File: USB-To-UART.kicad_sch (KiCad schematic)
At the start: 12 parts, among them Q1 NMOS, Q2 NMOS, U4 CH340X

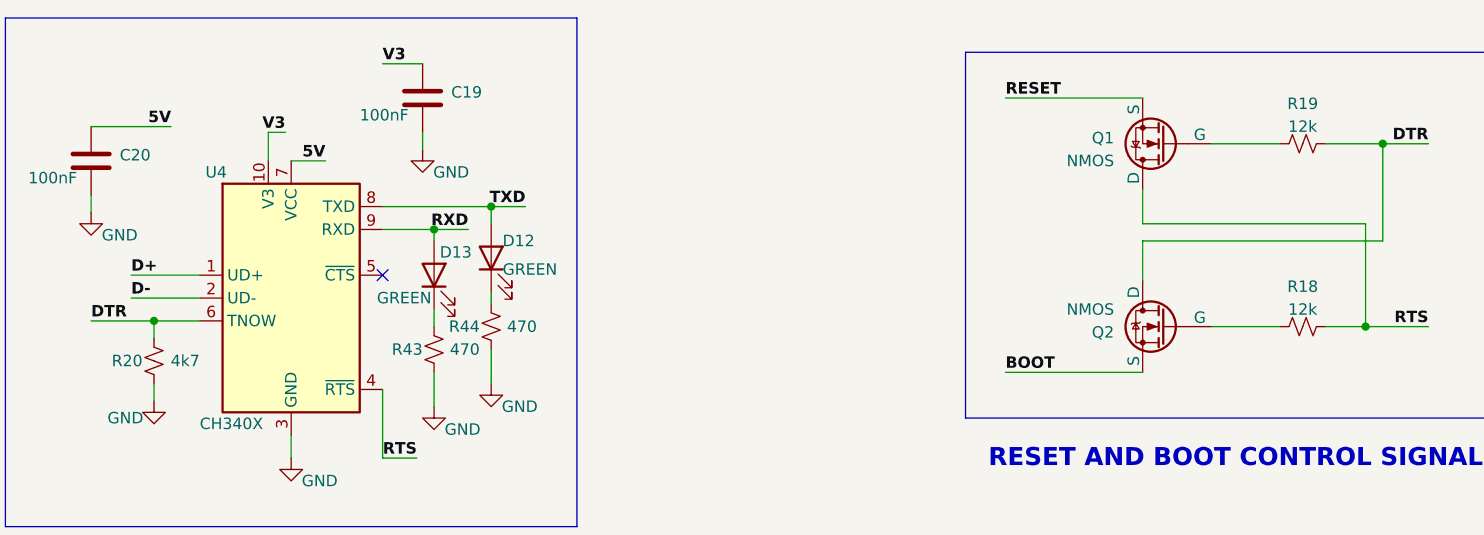
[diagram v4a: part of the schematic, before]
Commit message: Assigned footprints
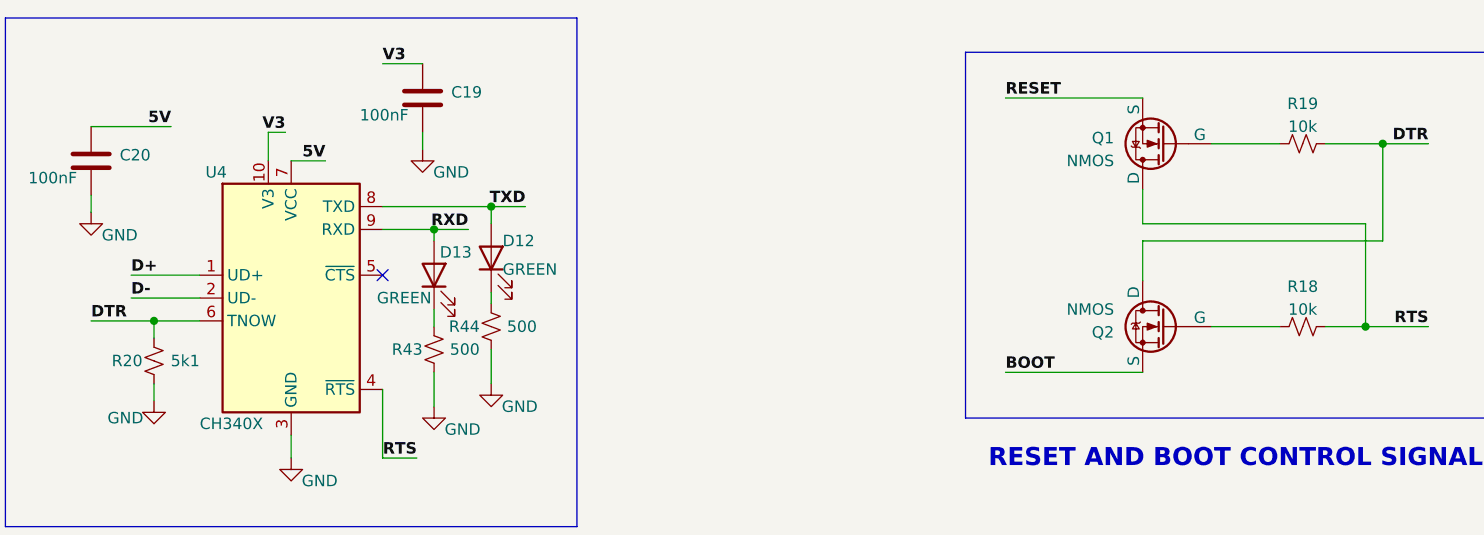
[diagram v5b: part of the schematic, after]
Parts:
- C19, C20: footprint ESP32-S3_DB:C_0402_1005Metric -> ESP32-S3_Dev_Board:C_0402_1005Metric
- D12, D13: footprint ESP32-S3_DB:LED_0603_1608Metric -> ESP32-S3_Dev_Board:LED_0603_1608Metric
- Q1, Q2: footprint (none) -> ESP32-S3_Dev_Board:SOT-23-3; PN (none) -> BSS138
- R18, R19: value 12k -> 10k; footprint (none) -> ESP32-S3_Dev_Board:R_0402_1005Metric; PN (none) -> RC0402FR-0710KL
- R20: value 4k7 -> 5k1; footprint (none) -> ESP32-S3_Dev_Board:R_0402_1005Metric; PN (none) -> RC0402FR-075K1L
- R43, R44: value 470 -> 500; footprint (none) -> ESP32-S3_Dev_Board:R_0402_1005Metric; PN (none) -> RC0402FR-07499RL
- U4: footprint Package_SO:MSOP-10_3x3mm_P0.5mm -> ESP32-S3_Dev_Board:MSOP-10_3x3mm_P0.5mm; PN (none) -> CH340X
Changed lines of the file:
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@@
       (effects (font (size 1.27 1.27)) (justify right))
     )
-    (property "Footprint" "ESP32-S3_DB:LED_0603_1608Metric" (at 116.84 95.885 0)
+    (property "Footprint" "ESP32-S3_Dev_Board:LED_0603_1608Metric" (at 116.84 95.885 0)
       (effects (font (size 1.27 1.27)) hide)
     )
@@
       (effects (font (size 1.27 1.27)) (justify left))
     )
-    (property "Value" "470" (at 128.27 101.6 0)
-      (effects (font (size 1.27 1.27)) (justify left))
-    )
-    (property "Footprint" "" (at 123.19 101.6 0)
+    (property "Value" "500" (at 128.27 101.6 0)
+      (effects (font (size 1.27 1.27)) (justify left))
+    )
+    (property "Footprint" "ESP32-S3_Dev_Board:R_0402_1005Metric" (at 123.19 101.6 0)
       (effects (font (size 1.27 1.27)) hide)
     )
@@
       (effects (font (size 1.27 1.27)) hide)
     )
+    (property "PN" "RC0402FR-07499RL" (at 123.19 101.6 0)
+      (effects (font (size 1.27 1.27)) hide)
+    )
     (pin "1")
     (pin "2")
@@
       (effects (font (size 1.27 1.27)) (justify left))
     )
-    (property "Value" "4k7" (at 90.805 105.41 0)
-      (effects (font (size 1.27 1.27)) (justify left))
-    )
-    (property "Footprint" "" (at 85.725 105.41 0)
+    (property "Value" "5k1" (at 90.805 105.41 0)
+      (effects (font (size 1.27 1.27)) (justify left))
+    )
+    (property "Footprint" "ESP32-S3_Dev_Board:R_0402_1005Metric" (at 85.725 105.41 0)
       (effects (font (size 1.27 1.27)) hide)
     )
@@
       (effects (font (size 1.27 1.27)) hide)
     )
+    (property "PN" "RC0402FR-075K1L" (at 85.725 105.41 0)
+      (effects (font (size 1.27 1.27)) hide)
+    )
     (pin "1")
     (pin "2")
@@
       (effects (font (size 1.27 1.27)) (justify left))
     )
-    (property "Value" "470" (at 121.92 104.14 0)
-      (effects (font (size 1.27 1.27)) (justify left))
-    )
-    (property "Footprint" "" (at 116.84 104.14 0)
+    (property "Value" "500" (at 121.92 104.14 0)
+      (effects (font (size 1.27 1.27)) (justify left))
+    )
+    (property "Footprint" "ESP32-S3_Dev_Board:R_0402_1005Metric" (at 116.84 104.14 0)
       (effects (font (size 1.27 1.27)) hide)
     )
@@
       (effects (font (size 1.27 1.27)) hide)
     )
+    (property "PN" "RC0402FR-07499RL" (at 116.84 104.14 0)
+      (effects (font (size 1.27 1.27)) hide)
+    )
     (pin "1")
     (pin "2")
@@
       (effects (font (size 1.27 1.27)) (justify left))
     )
-    (property "Footprint" "" (at 193.04 99.06 0)
+    (property "Footprint" "ESP32-S3_Dev_Board:SOT-23-3" (at 193.04 99.06 0)
       (effects (font (size 1.27 1.27)) hide)
     )
@@
     )
     (property "Sim.Pins" "1=D 2=G 3=S" (at 198.12 116.84 0)
+      (effects (font (size 1.27 1.27)) hide)
+    )
+    (property "PN" "BSS138" (at 198.12 101.6 0)
       (effects (font (size 1.27 1.27)) hide)
     )
@@
       (effects (font (size 1.27 1.27)) (justify left))
     )
-    (property "Footprint" "" (at 193.04 83.82 0)
+    (property "Footprint" "ESP32-S3_Dev_Board:SOT-23-3" (at 193.04 83.82 0)
       (effects (font (size 1.27 1.27)) hide)
     )
@@
     )
     (property "Sim.Pins" "1=D 2=G 3=S" (at 198.12 66.04 0)
+      (effects (font (size 1.27 1.27)) hide)
+    )
+    (property "PN" "BSS138" (at 198.12 81.28 0)
       (effects (font (size 1.27 1.27)) hide)
     )
@@
       (effects (font (size 1.27 1.27)))
     )
-    (property "Value" "12k" (at 213.36 79.375 90)
-      (effects (font (size 1.27 1.27)))
-    )
-    (property "Footprint" "" (at 213.36 81.28 0)
+    (property "Value" "10k" (at 213.36 79.375 90)
+      (effects (font (size 1.27 1.27)))
+    )
+    (property "Footprint" "ESP32-S3_Dev_Board:R_0402_1005Metric" (at 213.36 81.28 0)
       (effects (font (size 1.27 1.27)) hide)
     )
@@
       (effects (font (size 1.27 1.27)) hide)
     )
+    (property "PN" "RC0402FR-0710KL" (at 213.36 81.28 0)
+      (effects (font (size 1.27 1.27)) hide)
+    )
     (pin "1")
     (pin "2")
@@
       (effects (font (size 1.27 1.27)) (justify right))
     )
-    (property "Footprint" "ESP32-S3_DB:C_0402_1005Metric" (at 114.6048 72.39 0)
+    (property "Footprint" "ESP32-S3_Dev_Board:C_0402_1005Metric" (at 114.6048 72.39 0)
       (effects (font (size 1.27 1.27)) hide)
     )
@@
       (effects (font (size 1.27 1.27)))
     )
-    (property "Value" "12k" (at 213.36 99.695 90)
-      (effects (font (size 1.27 1.27)))
-    )
-    (property "Footprint" "" (at 213.36 101.6 0)
+    (property "Value" "10k" (at 213.36 99.695 90)
+      (effects (font (size 1.27 1.27)))
+    )
+    (property "Footprint" "ESP32-S3_Dev_Board:R_0402_1005Metric" (at 213.36 101.6 0)
       (effects (font (size 1.27 1.27)) hide)
     )
@@
       (effects (font (size 1.27 1.27)) hide)
     )
+    (property "PN" "RC0402FR-0710KL" (at 213.36 101.6 0)
+      (effects (font (size 1.27 1.27)) hide)
+    )
     (pin "1")
     (pin "2")
@@
       (effects (font (size 1.27 1.27)) (justify right))
     )
-    (property "Footprint" "ESP32-S3_DB:C_0402_1005Metric" (at 77.7748 79.375 0)
+    (property "Footprint" "ESP32-S3_Dev_Board:C_0402_1005Metric" (at 77.7748 79.375 0)
       (effects (font (size 1.27 1.27)) hide)
     )
@@
       (effects (font (size 1.27 1.27)) (justify right))
     )
-    (property "Footprint" "ESP32-S3_DB:LED_0603_1608Metric" (at 123.19 93.98 0)
+    (property "Footprint" "ESP32-S3_Dev_Board:LED_0603_1608Metric" (at 123.19 93.98 0)
       (effects (font (size 1.27 1.27)) hide)
     )
@@
       (effects (font (size 1.27 1.27)) (justify left))
     )
-    (property "Footprint" "Package_SO:MSOP-10_3x3mm_P0.5mm" (at 102.235 112.395 0)
+    (property "Footprint" "ESP32-S3_Dev_Board:MSOP-10_3x3mm_P0.5mm" (at 102.235 112.395 0)
       (effects (font (size 1.27 1.27)) (justify left) hide)
     )
@@
       (effects (font (size 1.27 1.27)) hide)
     )
+    (property "PN" "CH340X" (at 100.965 98.425 0)
+      (effects (font (size 1.27 1.27)) hide)
+    )

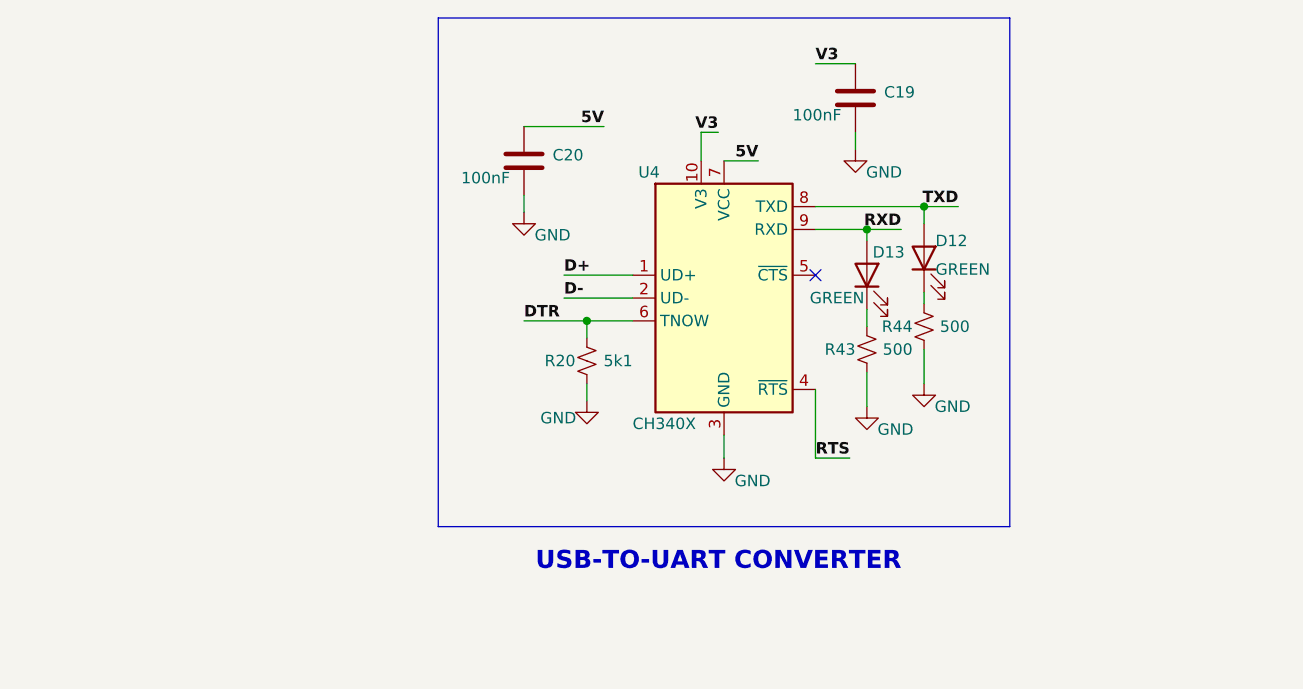
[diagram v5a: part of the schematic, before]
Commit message: Added bulk Decoupling and arranged components
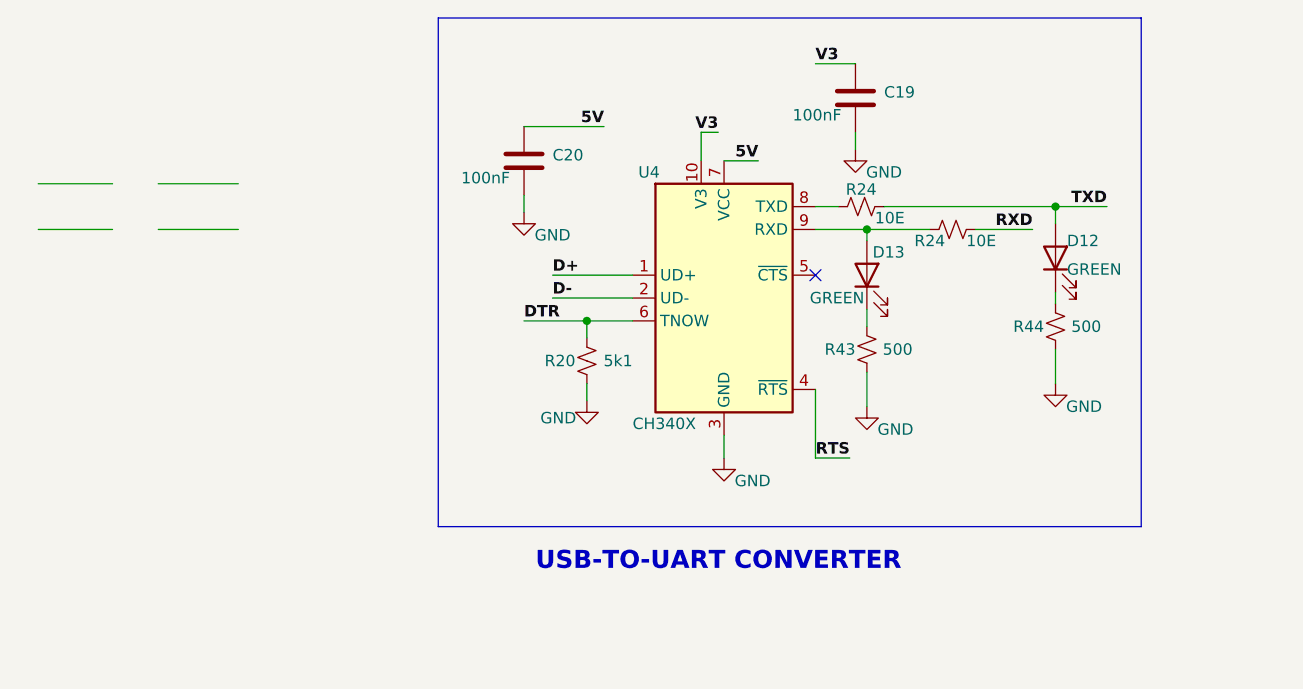
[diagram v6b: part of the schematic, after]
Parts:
- added R24 (x2): 10E, ESP32-S3_Dev_Board:R_0402_1005Metric, symbol ESP32-S3_DB:R_Small_US
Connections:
- net RXD: now also R24.2; no longer D13.2 (A), U4.9 (RXD)
- net TXD: now also R24.2; no longer U4.8 (TXD)
- new net: D13.2 (A), R24.1, U4.9 (RXD)
- new net: R24.1, U4.8 (TXD)
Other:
- moved on the sheet: D12, R44

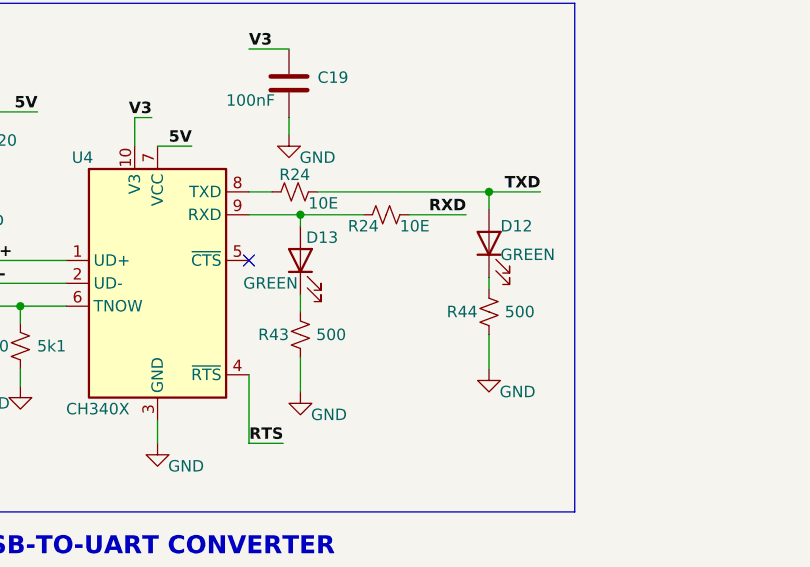
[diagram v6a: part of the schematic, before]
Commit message: Placed RS-485, CAN Transceiver and battery charger
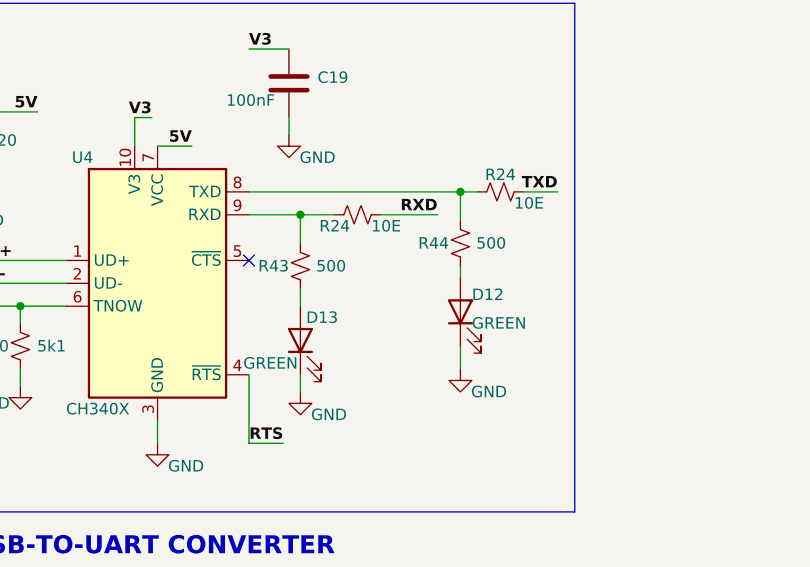
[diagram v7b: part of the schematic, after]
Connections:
- net GND: now also D12.1 (K), D13.1 (K); no longer R43.1, R44.1
- net TXD: no longer D12.2 (A)
- net at R43.2: now also R24.1, U4.9 (RXD); no longer D13.1 (K)
- net at R44.2: now also R24.1, U4.8 (TXD); no longer D12.1 (K)
- new net: D13.2 (A), R43.1
- new net: D12.2 (A), R44.1
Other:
- moved on the sheet: D12, D13, R24, R43, R44

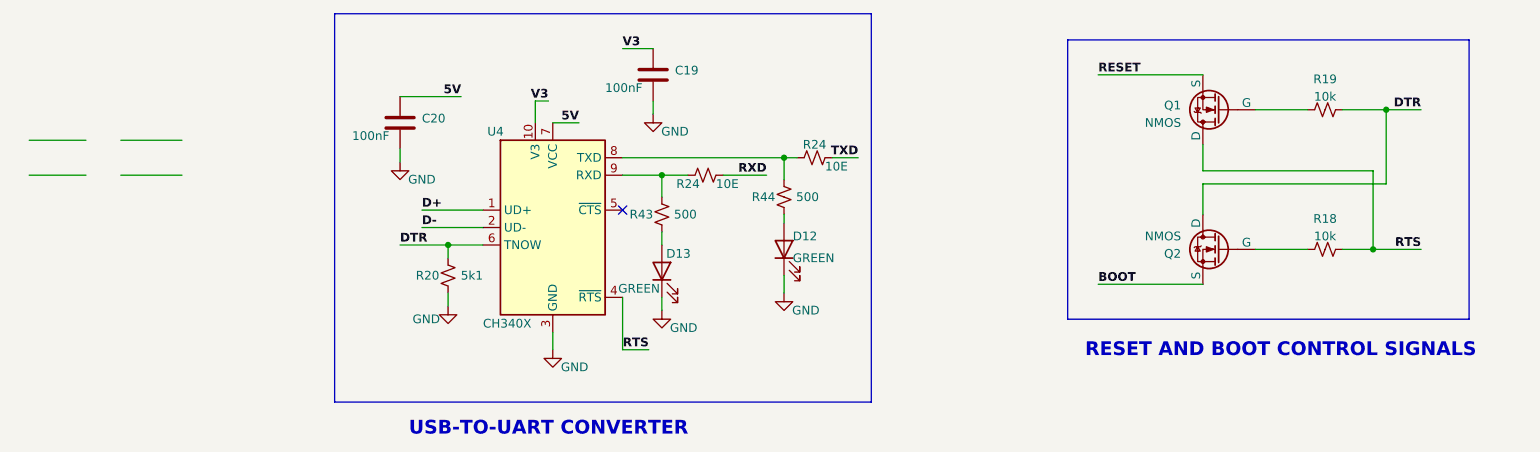
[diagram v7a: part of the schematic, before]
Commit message: Changes CH340 schematic
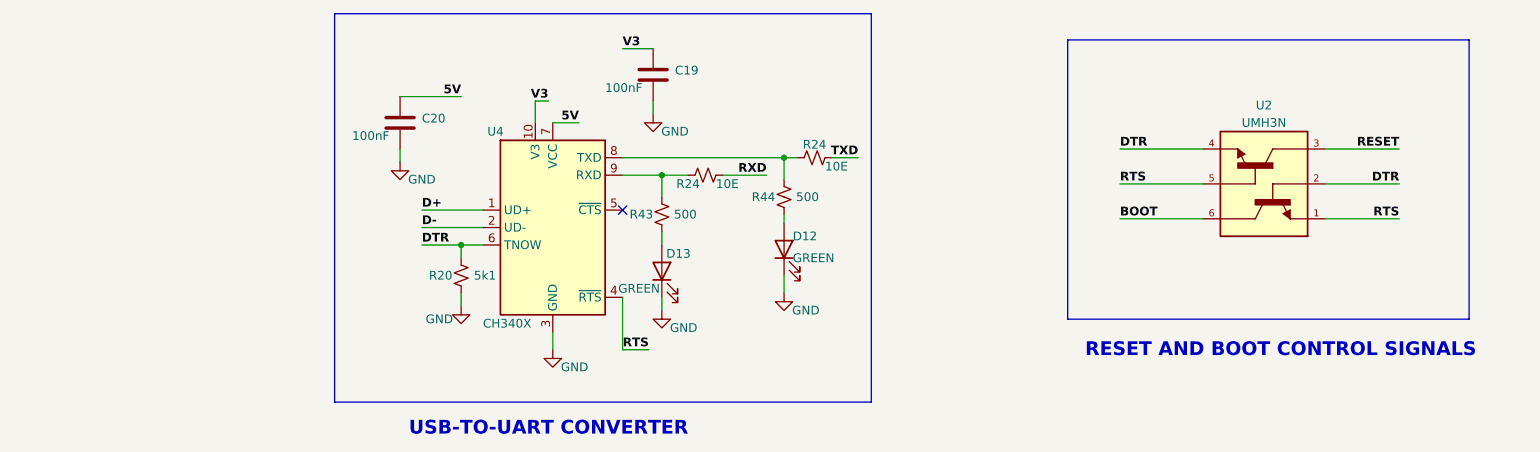
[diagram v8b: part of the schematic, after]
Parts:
- removed Q1, Q2: NMOS, ESP32-S3_Dev_Board:SOT-23-3, symbol ESP32-S3_DB:NMOS
- removed R18, R19: 10k, ESP32-S3_Dev_Board:R_0402_1005Metric, symbol ESP32-S3_DB:R_Small_US
- added U2: UMH3N, UMH3N:UMT6, symbol ESP32-S3_DB:UMH3N
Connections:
- net BOOT: now also U2.6
- net DTR: now also U2.2, U2.4
- net RESET: now also U2.3
- net RTS: now also U2.1, U2.5
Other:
- moved on the sheet: R20
